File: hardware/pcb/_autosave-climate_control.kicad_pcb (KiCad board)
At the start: 2 copper layers, 18 x 60 mm, 43 parts, among them J1 Switch, J2 BatteryIn, J3 USB_C, J4 HeatElement, J5 ICSP, Q1 NTR3C21NZ, Q2 NTR3C21NZ, U1 TP4056, U2 XB8089A, U3 ATmega328PB-AU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

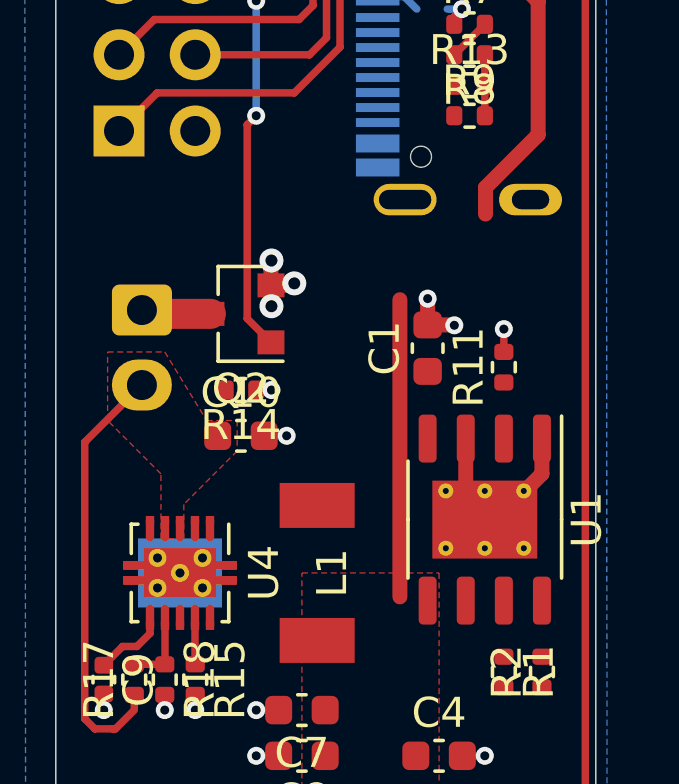
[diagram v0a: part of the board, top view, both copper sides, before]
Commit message: Removed resistor on TP4056.
Updated on PCB the routing.
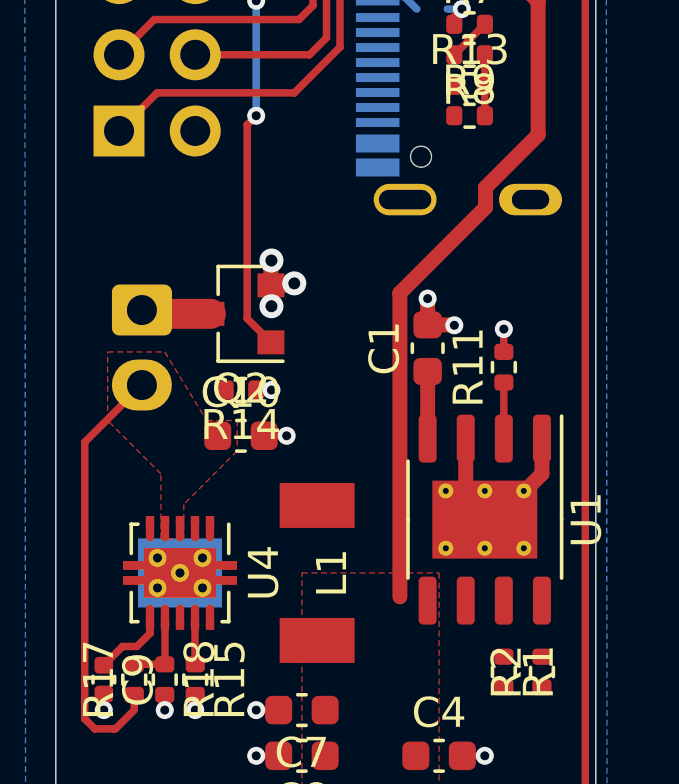
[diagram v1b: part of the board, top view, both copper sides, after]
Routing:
- net +BATT: track 44.0 -> 48.0 mm
- net Net-(C1-Pad1): track 0.00 -> 2.24 mm
- net Net-(R11-Pad1): track 0.00 -> 1.87 mm
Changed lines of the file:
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@@
     (thickness 1.6)
     (drawings 4)
-    (tracks 202)
+    (tracks 205)
     (zones 0)
     (modules 43)
@@
   )
   (setup
-    (last_trace_width 0.5)
+    (last_trace_width 0.25)
     (user_trace_width 0.5)
     (user_trace_width 1)
@@
   (segment (start 110.335 150.805) (end 109.375 151.765) (width 0.25) (layer F.Cu) (net 1))
   (segment (start 110.335 150.495) (end 110.335 150.805) (width 0.25) (layer F.Cu) (net 1))
+  (segment (start 112.395 130.65) (end 112.395 128.41) (width 0.5) (layer F.Cu) (net 2))
   (segment (start 106.674 102.62759) (end 108.263011 104.216601) (width 0.25) (layer F.Cu) (net 3))
   (segment (start 106.674 101.414) (end 106.674 102.62759) (width 0.25) (layer F.Cu) (net 3))
@@
   (segment (start 116.078 116.078) (end 116.078 120.526128) (width 0.5) (layer F.Cu) (net 5))
   (segment (start 116.078 120.526128) (end 114.32399 122.280138) (width 0.5) (layer F.Cu) (net 5))
-  (segment (start 111.46999 126.02001) (end 111.46999 135.92601) (width 0.5) (layer F.Cu) (net 5))
   (segment (start 115.284 107.758002) (end 115.316 107.790002) (width 0.5) (layer F.Cu) (net 5))
   (segment (start 115.284 107.664) (end 115.284 107.758002) (width 0.5) (layer F.Cu) (net 5))
   (segment (start 115.316 107.790002) (end 115.316 112.648128) (width 0.5) (layer F.Cu) (net 5))
-  (segment (start 114.32399 122.280138) (end 114.32399 123.16601) (width 0.5) (layer F.Cu) (net 5))
   (segment (start 115.316 112.648128) (end 114.3 113.664128) (width 0.5) (layer F.Cu) (net 5))
   (segment (start 114.3 114.423872) (end 114.3 113.664128) (width 0.5) (layer F.Cu) (net 5))
@@
   (via (at 107.188 105.41) (size 0.6) (drill 0.3) (layers F.Cu B.Cu) (net 5))
   (segment (start 107.188 105.41) (end 109.766003 105.41) (width 0.25) (layer B.Cu) (net 5))
+  (segment (start 114.32399 122.945008) (end 114.32399 122.280138) (width 0.5) (layer F.Cu) (net 5))
+  (segment (start 111.46999 125.799008) (end 114.32399 122.945008) (width 0.5) (layer F.Cu) (net 5))
+  (segment (start 111.46999 135.92601) (end 111.46999 125.799008) (width 0.5) (layer F.Cu) (net 5))
   (segment (start 113.832 106.172) (end 113.724 106.064) (width 0.25) (layer F.Cu) (net 6))
   (segment (start 115.598 106.172) (end 113.832 106.172) (width 0.25) (layer F.Cu) (net 6))
@@
   (segment (start 117.602 109.982) (end 116.332 108.712) (width 0.25) (layer F.Cu) (net 15))
   (segment (start 117.64999 109.982) (end 117.602 109.982) (width 0.25) (layer F.Cu) (net 15))
+  (segment (start 114.935 130.65) (end 114.935 128.78) (width 0.25) (layer F.Cu) (net 16))
   (via (at 106.68 116.055999) (size 0.6) (drill 0.3) (layers F.Cu B.Cu) (net 18))
   (segment (start 106.674 109.914) (end 106.674 116.049999) (width 0.25) (layer F.Cu) (net 18))
